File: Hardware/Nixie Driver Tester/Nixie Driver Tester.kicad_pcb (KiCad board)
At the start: 2 copper layers, 48.3 x 50.8 mm, 29 parts, among them J1 ICSP, J2 UJC-HP-3-SMT-TR, J3 OLED, J4 NIX3, J5 NIX1, J6 NIX2, Q1 MMBT2222A, Q2 MMBT2907ALT1G, Q3 FDD7N25LZTM, SW1 SW_Omron_B3FS

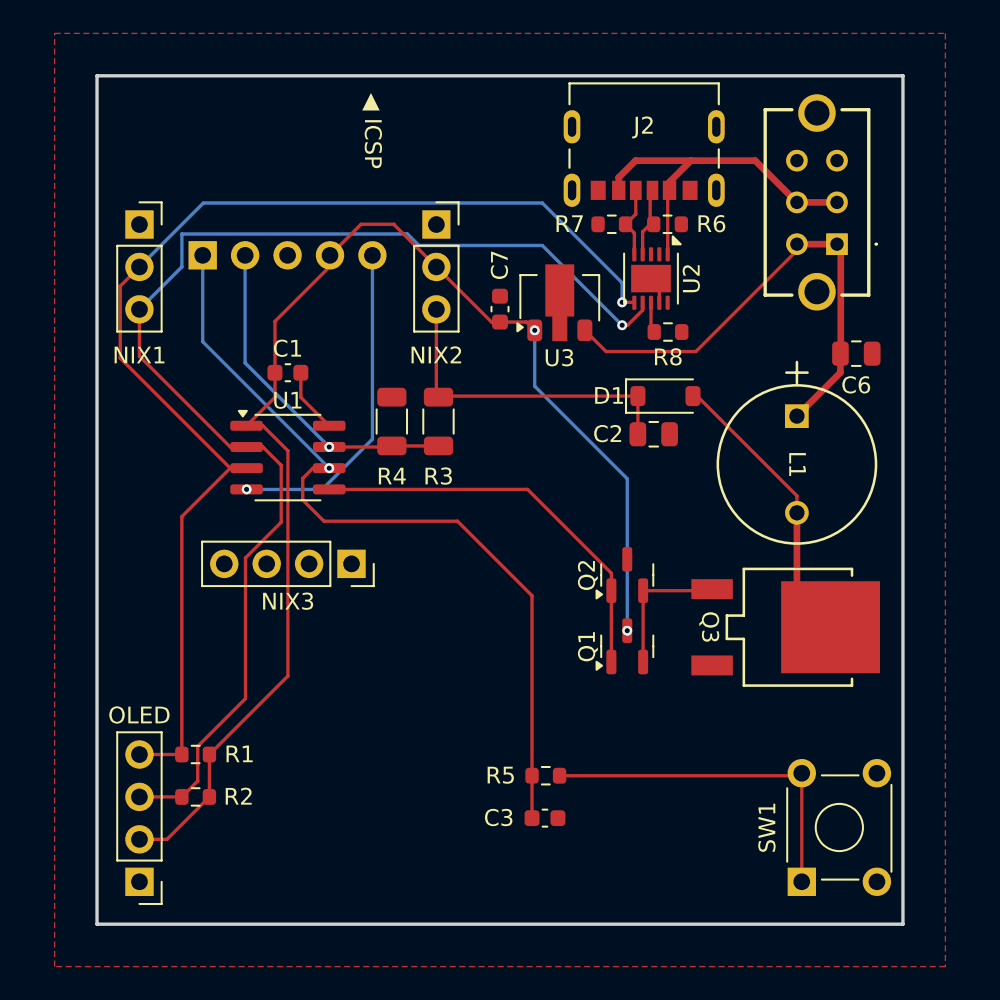
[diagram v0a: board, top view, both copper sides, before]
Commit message: Status LEDs and switch labels
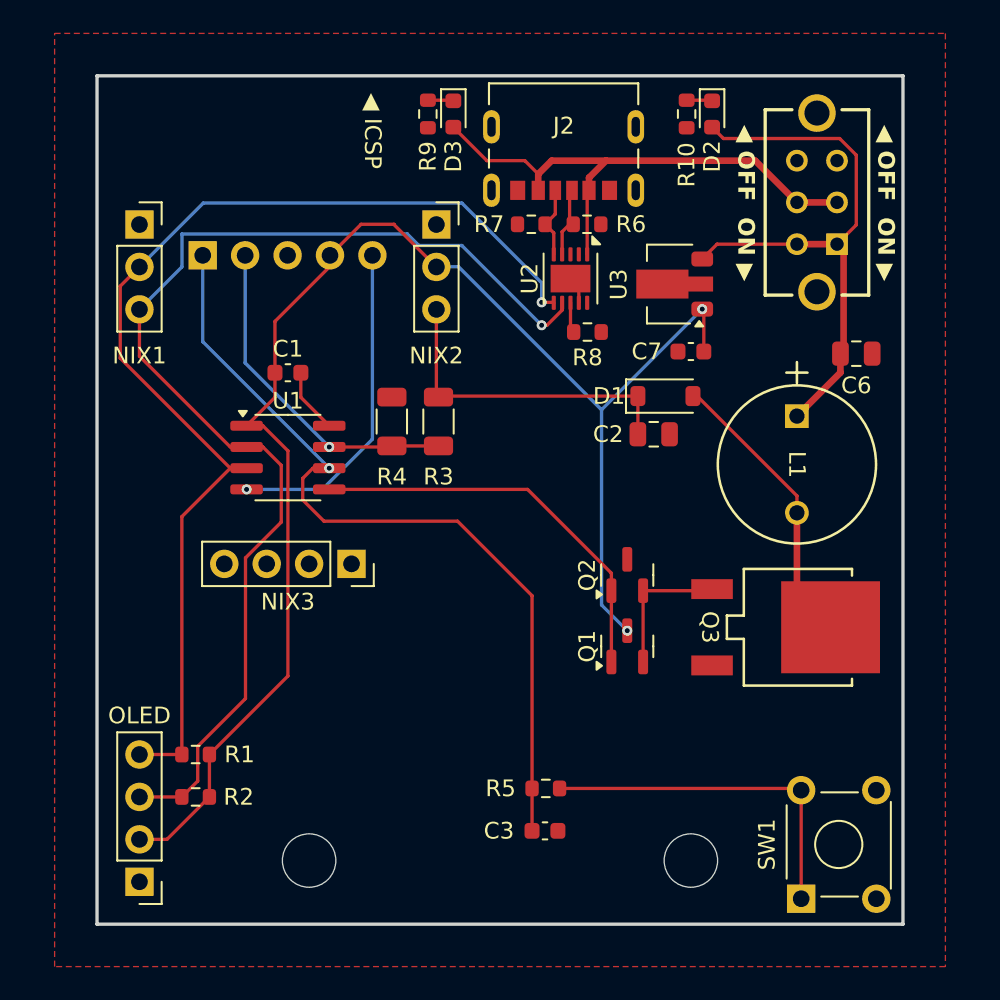
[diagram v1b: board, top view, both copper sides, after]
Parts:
- added D2: LED, LED_SMD:LED_0603_1608Metric, F.Cu at (160.0, 81.0)
- added D3: LED, LED_SMD:LED_0603_1608Metric, F.Cu at (144.5, 81.0)
- added R10: 49k, Resistor_SMD:R_0603_1608Metric, F.Cu at (158.5, 81.0)
- added R9: 49k, Resistor_SMD:R_0603_1608Metric, F.Cu at (143.0, 81.0)
- added REF**: MountingHole_3.2mm_M3, MountingHole:MountingHole_3.2mm_M3, F.Cu at (158.8, 125.7)
- added REF**: MountingHole_3.2mm_M3, MountingHole:MountingHole_3.2mm_M3, F.Cu at (135.9, 125.7)
- moved C7 11.7 mm to (158.8, 95.2), turned to 180 degrees
- moved U3 6.63 mm to (157.5, 91.2), turned to 180 degrees
- moved J2 4.82 mm to (151.1, 85.6)
- moved R6 4.82 mm to (152.5, 87.6)
- moved R8 4.82 mm to (152.6, 94.1)
- moved U2 4.82 mm to (151.5, 90.9)
- moved R7 4.82 mm to (149.2, 87.6)
- moved SW1 1.02 mm to (165.4, 128.0)
- moved C3 0.76 mm to (150.0, 124.0)
- moved R5 0.76 mm to (150.1, 121.4)
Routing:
- net /USB PD/VBUS In: track 21.5 -> 32.6 mm
- net /5V VRM/5V: track 79.2 -> 89.9 mm
- net /5V VRM/VBUS: track 30.0 -> 35.2 mm
- net /Controller/SDA: track 71.5 -> 66.7 mm
- net /Controller/SCL: track 75.1 -> 70.3 mm
- net Net-(D3-K): track 0.00 -> 1.54 mm
- net Net-(D2-K): track 0.00 -> 1.54 mm
- net /Button/Button: track 48.4 -> 49.2 mm
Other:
- board text added: "Nixie Driver Tester Aaron Johnson 02/04/2025"
- board text added: "◀ OFF ON ▶"

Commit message: One mounting hole
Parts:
- removed REF** (x2): MountingHole_3.2mm_M3, MountingHole:MountingHole_3.2mm_M3
- added H1: MountingHole, MountingHole:MountingHole_3.2mm_M3, F.Cu at (125.7, 104.1)
- moved C1 3.42 mm to (131.4, 97.8), turned to 180 degrees
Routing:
- net GND: track 5.54 -> 14.3 mm
- net /5V VRM/5V: track 89.9 -> 90.8 mm
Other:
- board size 48.3 x 50.8 mm -> 50.8 x 50.8 mm

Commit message: Two mounting holes
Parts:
- added H2: MountingHole, MountingHole:MountingHole_3.2mm_M3, F.Cu at (168.9, 104.1)
- moved L1 5.08 mm to (160.0, 99.1)
- moved C6 3.56 mm to (165.1, 95.4)
- moved D1 3.56 mm to (153.7, 97.9)
- moved C2 3.49 mm to (153.0, 100.2)
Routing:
- net /Boost Converter/180V: track 19.3 -> 16.0 mm
- net Net-(D1-A): track 17.8 -> 20.1 mm
- net /5V VRM/VBUS: track 35.2 -> 36.6 mm

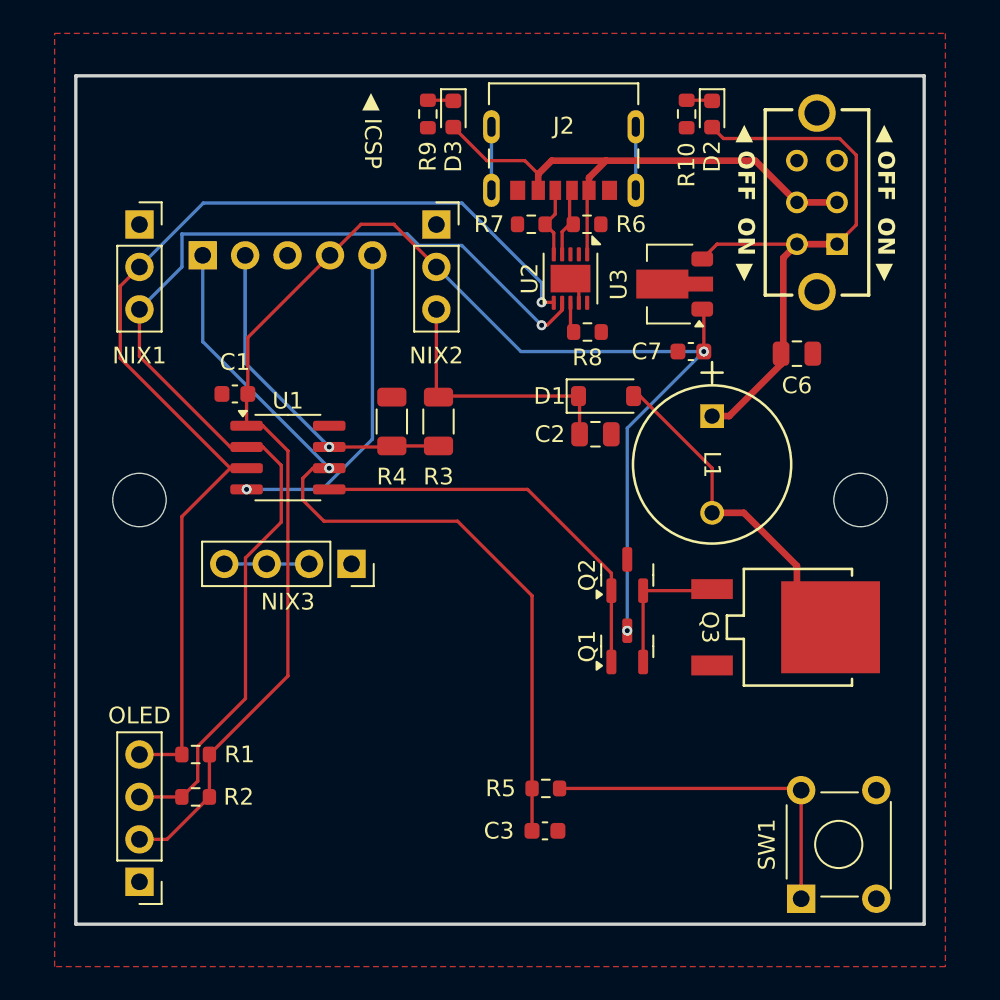
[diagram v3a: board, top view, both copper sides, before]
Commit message: Moved L for visibility
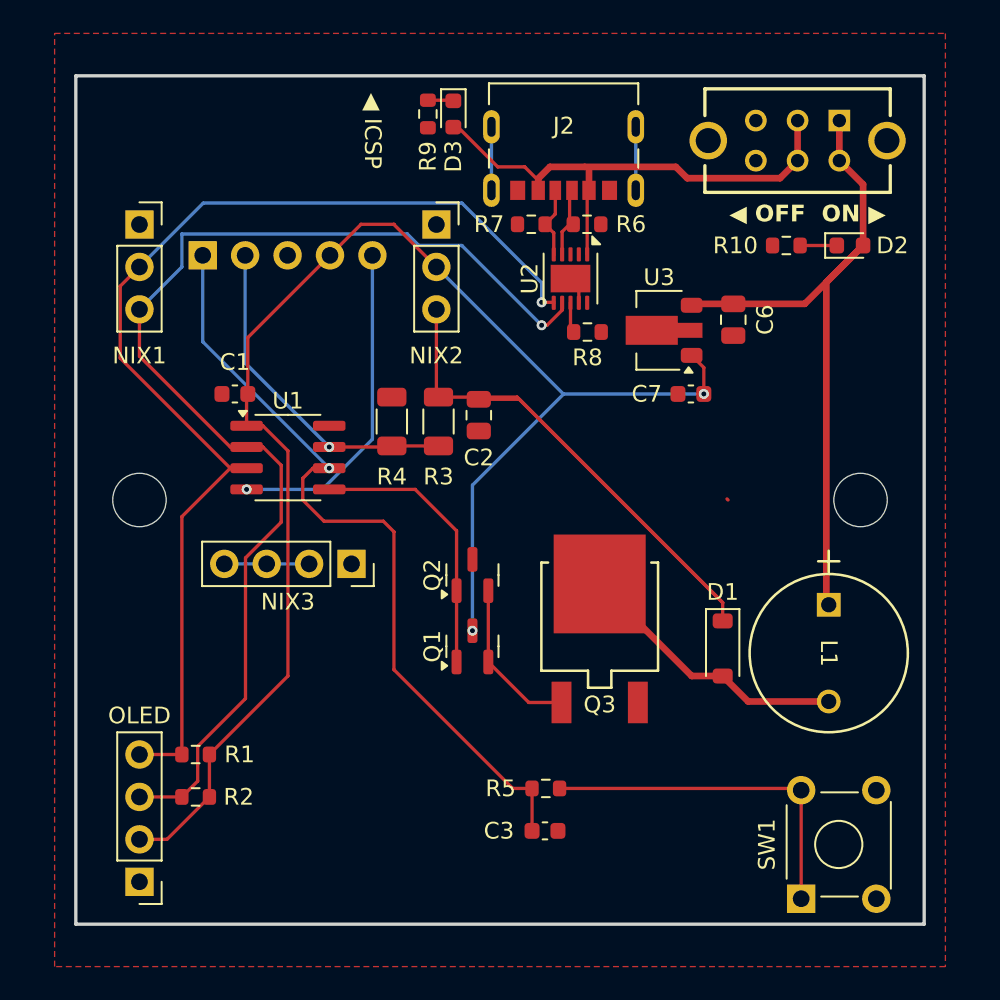
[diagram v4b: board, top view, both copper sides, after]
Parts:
- moved D1 16.6 mm to (160.7, 113.0), turned to -90 degrees
- moved L1 13.3 mm to (167.0, 110.4)
- moved Q3 11.9 mm to (153.3, 111.1), turned to 0 degrees
- moved D2 11.4 mm to (168.3, 88.9), turned to 0 degrees
- moved R10 9.88 mm to (164.5, 88.9), turned to 180 degrees
- moved Q1 9.27 mm to (145.7, 112.9)
- moved Q2 9.27 mm to (145.7, 108.6)
- moved S1 7.40 mm to (167.6, 81.4), turned to 180 degrees
- moved C2 7.08 mm to (146.1, 99.1), turned to -90 degrees
- moved C6 4.32 mm to (161.3, 93.3), turned to -90 degrees
- moved U3 2.84 mm to (156.8, 94.0)
- moved C7 2.54 mm to (158.8, 97.8)
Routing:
- net /Boost Converter/180V: track 16.0 -> 48.2 mm
- net /Boost Converter/PWM: track 24.3 -> 16.5 mm
- net /5V VRM/VBUS: track 36.6 -> 42.3 mm
- net Net-(D1-A): track 20.1 -> 16.6 mm
- net /Button/Button: track 49.2 -> 47.3 mm
- net Net-(Q1-E): track 8.44 -> 9.66 mm
- net /5V VRM/5V: track 90.8 -> 89.7 mm
- net Net-(D2-K): track 1.54 -> 2.20 mm
- net /USB PD/VBUS In: track 32.6 -> 32.0 mm

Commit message: Major layout change to get the L out of the way
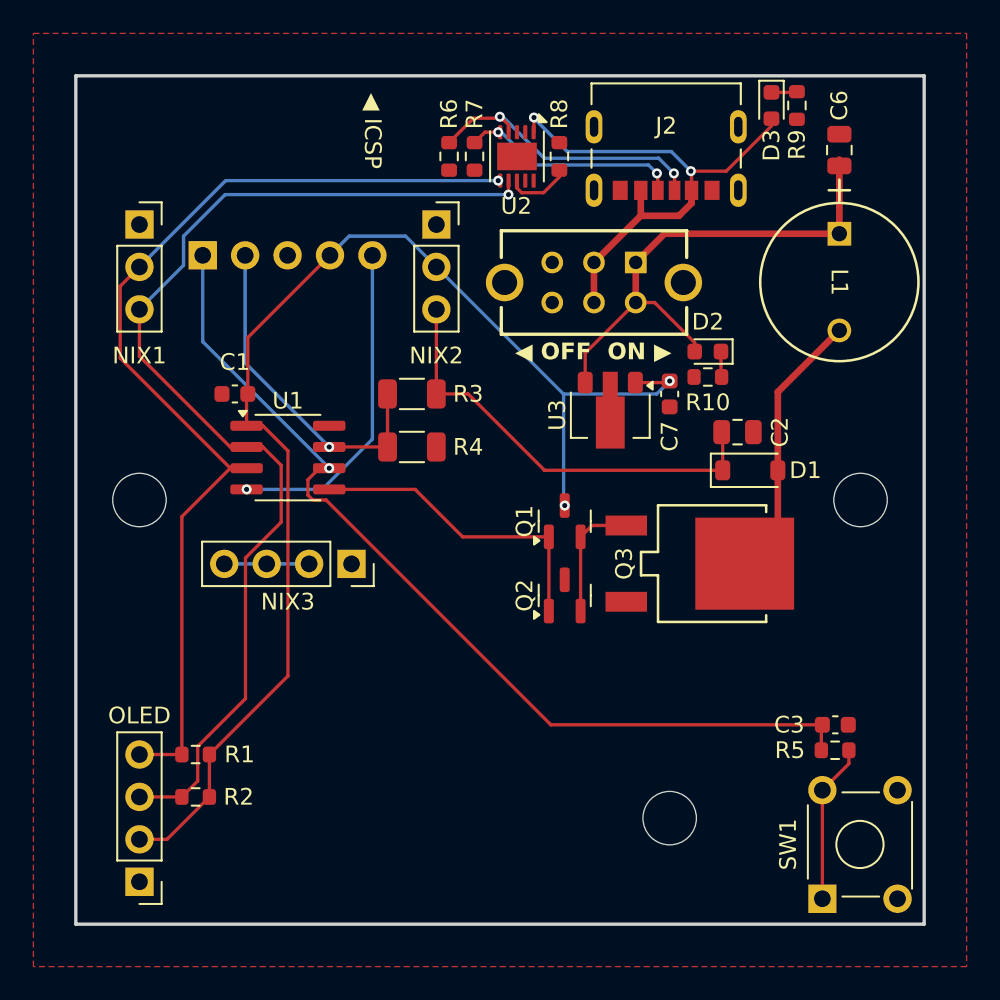
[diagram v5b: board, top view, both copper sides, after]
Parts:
- added H3: MountingHole, MountingHole:MountingHole_3.2mm_M3, F.Cu at (157.5, 123.2)
- moved L1 22.2 mm to (167.6, 88.2)
- moved R9 22.1 mm to (165.1, 80.5)
- moved D3 19.1 mm to (163.6, 80.5)
- moved C3 18.5 mm to (167.4, 117.6)
- moved R5 17.5 mm to (167.4, 119.1)
- moved C2 15.5 mm to (161.5, 100.1), turned to 0 degrees
- moved S1 14.9 mm to (155.4, 89.9)
- moved C6 12.0 mm to (167.6, 83.2), turned to 90 degrees
- moved D1 10.8 mm to (162.3, 102.4), turned to 0 degrees
- moved R8 10.6 mm to (150.9, 83.6), turned to 90 degrees
- moved D2 10.6 mm to (159.8, 95.2), turned to 180 degrees
- moved Q1 9.31 mm to (151.2, 105.4)
- moved R6 9.20 mm to (144.3, 83.6), turned to 90 degrees
- moved R10 9.17 mm to (159.8, 96.8)
- moved U2 7.99 mm to (148.3, 83.6)
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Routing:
- net /Boost Converter/180V: track 48.2 -> 26.4 mm
- net /USB PD/CC1: track 4.08 -> 17.7 mm, vias 0 -> 2
- net /5V VRM/5V: track 89.7 -> 77.1 mm
- net Net-(R5-Pad2): track 21.0 -> 9.55 mm
- net /5V VRM/VBUS: track 42.3 -> 30.9 mm
- net GND: track 14.4 -> 5.08 mm
- net /Button/Button: track 47.3 -> 56.4 mm
- net /USB PD/CC2: track 4.30 -> 13.4 mm, vias 0 -> 2
- net /Controller/SDA: track 66.7 -> 60.7 mm
- net /Controller/SCL: track 70.3 -> 65.7 mm
- net /Boost Converter/PWM: track 16.5 -> 18.8 mm
- net Net-(Q1-E): track 9.66 -> 7.46 mm
- net Net-(U2-VSET): track 1.83 -> 3.89 mm
- net /USB PD/VBUS In: track 32.0 -> 31.2 mm, vias 0 -> 2
- net Net-(D2-K): track 2.20 -> 1.54 mm

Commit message: Shrink the board a bit.
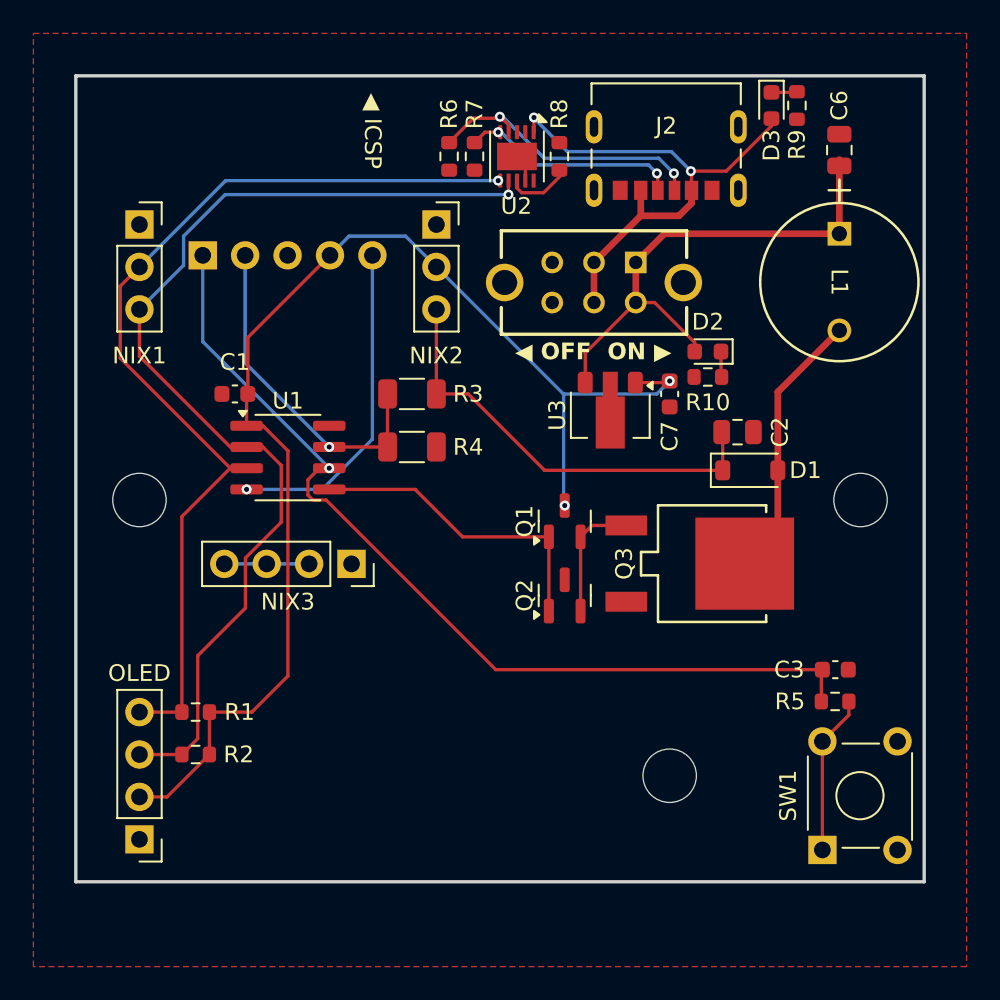
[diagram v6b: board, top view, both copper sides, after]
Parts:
- moved C3 3.30 mm to (167.4, 114.3)
- moved R5 2.92 mm to (167.4, 116.2)
- moved SW1 2.92 mm to (166.6, 125.1)
- moved J3 2.54 mm to (125.7, 124.5)
- moved R2 2.54 mm to (129.1, 119.4)
- moved H3 2.54 mm to (157.5, 120.7)
- moved R1 2.54 mm to (129.1, 116.8)
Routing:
- net /Controller/SCL: track 65.7 -> 63.1 mm
- net /Controller/SDA: track 60.7 -> 58.2 mm
- net GND: track 5.08 -> 6.74 mm
- net /5V VRM/5V: track 77.1 -> 76.1 mm
- net /Button/Button: track 56.4 -> 55.4 mm
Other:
- board size 50.8 x 50.8 mm -> 50.8 x 48.3 mm

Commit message: Switched to custom OLED symbol/footprint
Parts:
- J3: footprint Connector_PinHeader_2.54mm:PinHeader_1x04_P2.54mm_Vertical -> Display_:SSD1306 0.91 128x32 OLED
- turned J3 to 0 degrees

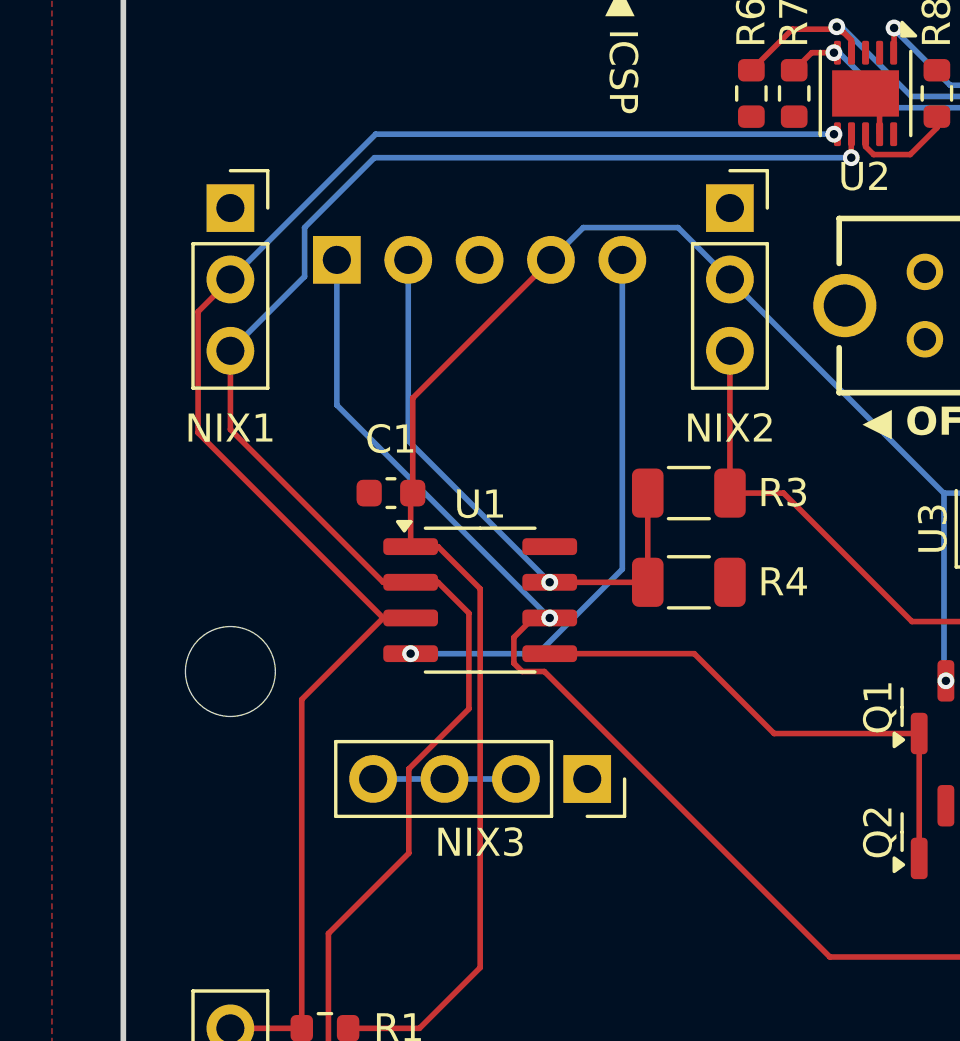
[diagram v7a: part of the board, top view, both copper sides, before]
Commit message: Switched to custom nixie driver symbol/footprint
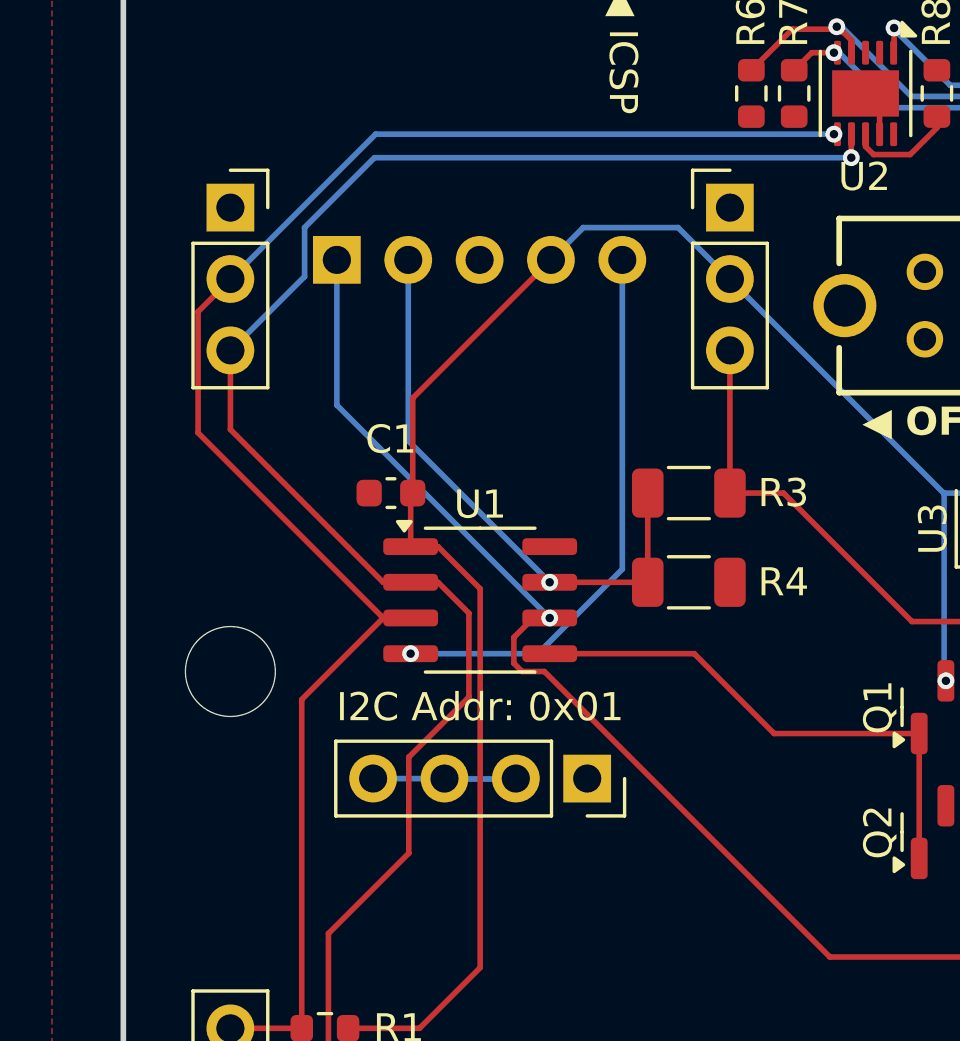
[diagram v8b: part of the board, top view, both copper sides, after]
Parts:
- removed J4: NIX3, Connector_PinSocket_2.54mm:PinSocket_1x04_P2.54mm_Vertical
- removed J5: NIX1, Connector_PinSocket_2.54mm:PinSocket_1x03_P2.54mm_Vertical
- removed J6: NIX2, Connector_PinSocket_2.54mm:PinSocket_1x03_P2.54mm_Vertical
- added N1: Nixie, Nixie:Nixie Driver V2, F.Cu at (134.6, 95.2)
